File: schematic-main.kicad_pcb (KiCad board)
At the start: 2 copper layers, 97.6 x 72.5 mm, 92 parts, among them IC1 LM76202QPWPRQ1, J1 Conn_01x02, J2 Conn_01x03, J3 Conn_01x03_Pin, J6 Conn_01x04, P1 USB_C_Plug_USB2.0, U2 TPS62933, U3 USBLC6-2P6, U4 ESP32-S3FN8, U5 SN65HVD232, U6 PC817, U7 PC817, Y1 Crystal_GND24

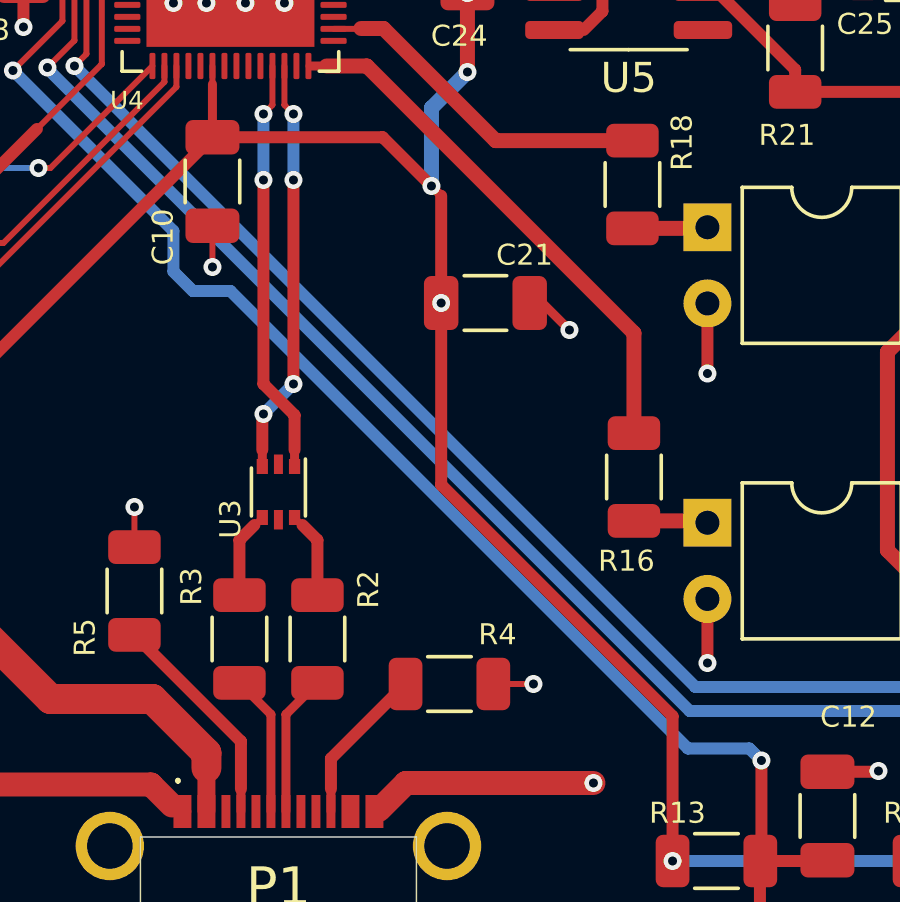
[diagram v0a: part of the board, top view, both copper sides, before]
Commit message: Fixing mistake in control of USB at PCB layout
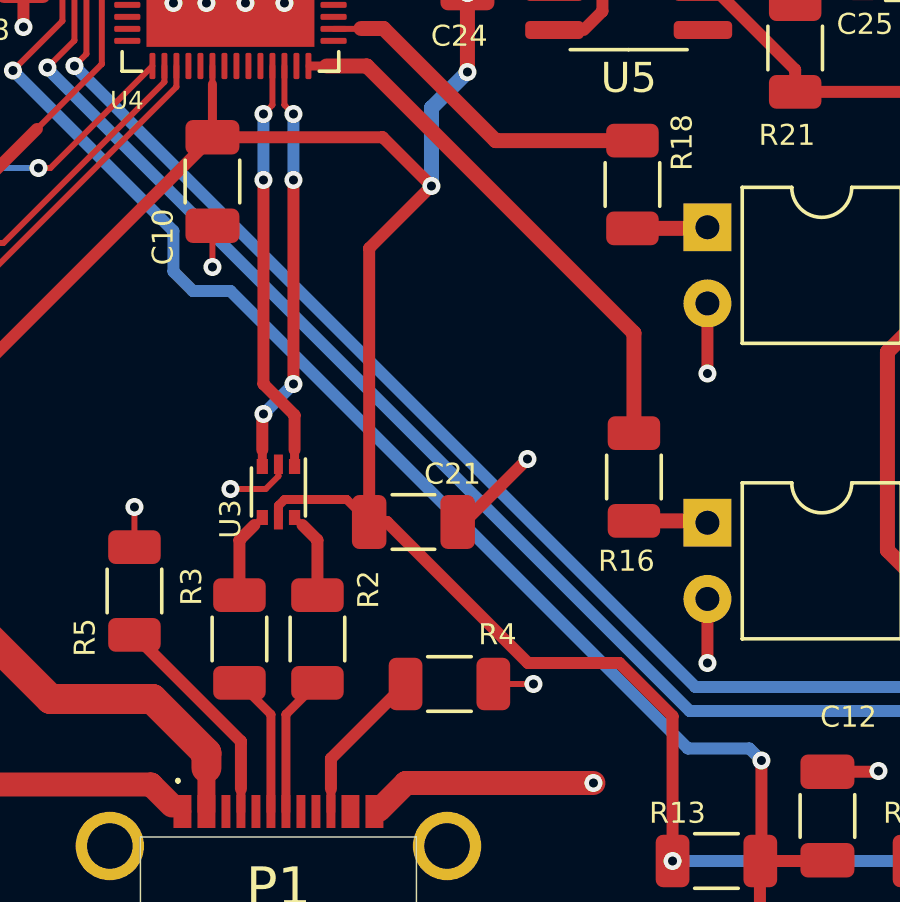
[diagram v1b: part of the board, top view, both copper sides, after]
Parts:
- moved C21 7.68 mm to (107.1, 107.6)
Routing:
- net +3.3V: track 215.0 -> 222.6 mm, vias 11 -> 10
- net GND: track 114.7 -> 118.3 mm, vias 51 -> 52
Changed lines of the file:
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@@
   )
   (footprint "Capacitor_SMD:C_1206_3216Metric" (layer "F.Cu")
-    (at 109.5 100.3)
+    (at 107.1 107.6)
     (descr "Capacitor SMD 1206 (3216 Metric), square (rectangular) end terminal, IPC_7351 nominal, (Body size source: IPC-SM-782 page 76, https://www.pcb-3d.com/wordpress/wp-content/uploads/ipc-sm-782a_amendment_1_and_2.pdf), generated with kicad-footprint-generator")
     (tags "capacitor")
@@
   (segment (start 126.0125 80.4) (end 127.8 80.4) (width 0.4) (layer "F.Cu") (net 2))
   (segment (start 128.8 115.925) (end 130.475 115.925) (width 0.4) (layer "F.Cu") (net 2))
-  (segment (start 110.975 100.3) (end 111.4 100.3) (width 0.3) (layer "F.Cu") (net 2))
   (segment (start 99.25 78.1375) (end 99.25 78.4375) (width 0.2) (layer "F.Cu") (net 2))
   (segment (start 100.4 97.725) (end 100.4 99.1) (width 0.2) (layer "F.Cu") (net 2))
   (segment (start 97.975 82.1375) (end 96.6375 82.1375) (width 0.15) (layer "F.Cu") (net 2))
   (segment (start 101.1625 88.9625) (end 101.2 89) (width 0.15) (layer "F.Cu") (net 2))
+  (segment (start 102.6 105.675) (end 102.6 106.074264) (width 0.2) (layer "F.Cu") (net 2))
   (segment (start 115.737 64.9) (end 114.762 65.875) (width 0.4) (layer "F.Cu") (net 2))
   (segment (start 108.5 58.825) (end 106.825 58.825) (width 0.3) (layer "F.Cu") (net 2))
@@
   (segment (start 108.9 87.02) (end 107.27 87.02) (width 0.4) (layer "F.Cu") (net 2))
   (segment (start 92.125 80.8) (end 92.125 78.925) (width 0.4) (layer "F.Cu") (net 2))
-  (segment (start 111.4 100.3) (end 112.3 101.2) (width 0.3) (layer "F.Cu") (net 2))
   (segment (start 97.975 79.7125) (end 97.975 82.1375) (width 0.3) (layer "F.Cu") (net 2))
   (segment (start 92.125 78.925) (end 92.15 78.9) (width 0.2) (layer "F.Cu") (net 2))
   (segment (start 99.25 117.25) (end 99.05 117.05) (width 0.3) (layer "F.Cu") (net 2))
+  (segment (start 108.8 107.6) (end 110.9 105.5) (width 0.4) (layer "F.Cu") (net 2))
   (segment (start 111.824 66.2) (end 114.437 66.2) (width 0.4) (layer "F.Cu") (net 2))
   (segment (start 106.825 58.825) (end 106.8 58.8) (width 0.3) (layer "F.Cu") (net 2))
@@
   (segment (start 123 64.825) (end 123 63.4) (width 0.3) (layer "F.Cu") (net 2))
   (segment (start 99.25 78.1375) (end 99.25 77.9375) (width 0.2) (layer "F.Cu") (net 2))
+  (segment (start 102.174264 106.5) (end 101 106.5) (width 0.2) (layer "F.Cu") (net 2))
   (segment (start 94.1 89.725) (end 94.1 91.1) (width 0.4) (layer "F.Cu") (net 2))
   (segment (start 81.15 64.7875) (end 81.15 63.4) (width 0.3) (layer "F.Cu") (net 2))
@@
   (segment (start 115.087 66.2) (end 114.762 65.875) (width 0.4) (layer "F.Cu") (net 2))
   (segment (start 92.1 116.35) (end 92.1 116.4) (width 0.8) (layer "F.Cu") (net 2))
+  (segment (start 108.575 107.6) (end 108.8 107.6) (width 0.4) (layer "F.Cu") (net 2))
   (segment (start 117.7 66.2) (end 115.087 66.2) (width 0.4) (layer "F.Cu") (net 2))
   (segment (start 116.821814 63.6) (end 114.762 65.659814) (width 0.4) (layer "F.Cu") (net 2))
@@
   (segment (start 110.54 88.66) (end 111.8 88.66) (width 0.4) (layer "F.Cu") (net 2))
   (segment (start 115 58.8375) (end 116.6625 58.8375) (width 0.3) (layer "F.Cu") (net 2))
+  (segment (start 102.6 106.074264) (end 102.174264 106.5) (width 0.2) (layer "F.Cu") (net 2))
   (segment (start 125.8625 75.8) (end 127.45 75.8) (width 0.4) (layer "F.Cu") (net 2))
   (segment (start 116.9 110.165) (end 116.9 112.3) (width 0.4) (layer "F.Cu") (net 2))
@@
   (via (at 81.15 63.4) (size 0.6) (drill 0.3) (layers "F.Cu" "B.Cu") (net 2))
   (via (at 104.8 73.1) (size 0.6) (drill 0.3) (layers "F.Cu" "B.Cu") (net 2))
-  (via (at 112.3 101.2) (size 0.6) (drill 0.3) (layers "F.Cu" "B.Cu") (net 2))
   (via (at 97.8 107.1) (size 0.6) (drill 0.3) (layers "F.Cu" "B.Cu") (net 2))
   (via (at 100.4 99.1) (size 0.6) (drill 0.3) (layers "F.Cu" "B.Cu") (net 2))
@@
   (via (at 99.1 90.3) (size 0.6) (drill 0.3) (layers "F.Cu" "B.Cu") (net 2))
   (via (at 138.6 115.9) (size 0.6) (drill 0.3) (layers "F.Cu" "B.Cu") (net 2))
+  (via (at 110.9 105.5) (size 0.6) (drill 0.3) (layers "F.Cu" "B.Cu") (net 2))
   (via (at 116.9 102.65) (size 0.6) (drill 0.3) (layers "F.Cu" "B.Cu") (net 2))
   (via (at 101.5 88.7) (size 0.6) (drill 0.3) (layers "F.Cu" "B.Cu") (net 2))
@@
   (via (at 103.3 59.6) (size 0.6) (drill 0.3) (layers "F.Cu" "B.Cu") (net 2))
   (via (at 100.2 90.3) (size 0.6) (drill 0.3) (layers "F.Cu" "B.Cu") (net 2))
+  (via (at 101 106.5) (size 0.6) (drill 0.3) (layers "F.Cu" "B.Cu") (net 2))
   (via (at 125.05 91.005) (size 0.6) (drill 0.3) (layers "F.Cu" "B.Cu") (net 2))
   (via (at 94.5 63.45) (size 0.6) (drill 0.3) (layers "F.Cu" "B.Cu") (net 2))
@@
   (segment (start 73.275 66.865) (end 73.29 66.85) (width 0.5) (layer "F.Cu") (net 5))
   (segment (start 73.29 68.035) (end 73.275 68.05) (width 0.2) (layer "F.Cu") (net 5))
-  (segment (start 108.025 96.725) (end 108.025 100.3) (width 0.4) (layer "F.Cu") (net 6))
-  (segment (start 115.7375 114.07255) (end 108.025 106.36005) (width 0.4) (layer "F.Cu") (net 6))
+  (segment (start 102.6 107.525) (end 102.6 107.055024) (width 0.3) (layer "F.Cu") (net 6))
+  (segment (start 105.625 107.6) (end 106.21924 107.6) (width 0.4) (layer "F.Cu") (net 6))
   (segment (start 94.475 72.575) (end 94.5 72.55) (width 0.2) (layer "F.Cu") (net 6))
+  (segment (start 102.805024 106.85) (end 104.875 106.85) (width 0.3) (layer "F.Cu") (net 6))
+  (segment (start 102.6 107.055024) (end 102.805024 106.85) (width 0.3) (layer "F.Cu") (net 6))
   (segment (start 100.4 94.775) (end 100.4 93) (width 0.3) (layer "F.Cu") (net 6))
   (segment (start 87.8 72.6) (end 87.8 76.4) (width 1) (layer "F.Cu") (net 6))
   (segment (start 97.6 83.7) (end 95.075 83.7) (width 0.4) (layer "F.Cu") (net 6))
+  (segment (start 106.21924 107.6) (end 110.91924 112.3) (width 0.4) (layer "F.Cu") (net 6))
   (segment (start 78.625 72.65) (end 78.65 72.675) (width 0.2) (layer "F.Cu") (net 6))
   (segment (start 107 71.7) (end 98.8 71.7) (width 0.8) (layer "F.Cu") (net 6))
@@
   (segment (start 79.4 86.8) (end 86.075 86.8) (width 0.4) (layer "F.Cu") (net 6))
   (segment (start 98.4 84.5) (end 97.6 83.7) (width 0.4) (layer "F.Cu") (net 6))
+  (segment (start 113.96495 112.3) (end 115.7375 114.07255) (width 0.4) (layer "F.Cu") (net 6))
   (segment (start 98.8 85.45) (end 98.4 85.05) (width 0.2) (layer "F.Cu") (net 6))
   (segment (start 108.9 92.6) (end 108.9 89.97) (width 0.5) (layer "F.Cu") (net 6))
   (segment (start 108.9 89.97) (end 111.76 89.97) (width 0.4) (layer "F.Cu") (net 6))
-  (segment (start 107.7 96.4) (end 108.025 96.725) (width 0.3) (layer "F.Cu") (net 6))
   (segment (start 106.075 94.775) (end 100.4 94.775) (width 0.4) (layer "F.Cu") (net 6))
   (segment (start 131.7375 118.9) (end 131.7 118.9) (width 0.4) (layer "F.Cu") (net 6))
@@
   (segment (start 78.575 72.7) (end 78.65 72.775) (width 0.2) (layer "F.Cu") (net 6))
   (segment (start 81.1875 72.675) (end 81.2 72.6625) (width 0.2) (layer "F.Cu") (net 6))
+  (segment (start 110.91924 112.3) (end 113.96495 112.3) (width 0.4) (layer "F.Cu") (net 6))
   (segment (start 79.125 78.6) (end 81.8 78.6) (width 0.5) (layer "F.Cu") (net 6))
   (segment (start 95.075 80.8) (end 95.075 78.675) (width 0.4) (layer "F.Cu") (net 6))
@@
   (segment (start 75.075 78.6) (end 79.125 78.6) (width 0.4) (layer "F.Cu") (net 6))
   (segment (start 94.5 72.55) (end 87.85 72.55) (width 0.4) (layer "F.Cu") (net 6))
-  (segment (start 108.025 106.36005) (end 108.025 100.3) (width 0.4) (layer "F.Cu") (net 6))
+  (segment (start 105.625 98.475) (end 105.625 107.6) (width 0.4) (layer "F.Cu") (net 6))
   (segment (start 111.76 89.97) (end 111.8 89.93) (width 0.2) (layer "F.Cu") (net 6))
   (segment (start 100.4 92.4) (end 100.4 93) (width 0.2) (layer "F.Cu") (net 6))
+  (segment (start 107.7 96.4) (end 105.625 98.475) (width 0.4) (layer "F.Cu") (net 6))
   (segment (start 87.8 76.4) (end 88.45 77.05) (width 0.8) (layer "F.Cu") (net 6))
   (segment (start 87.85 72.55) (end 87.8 72.6) (width 0.2) (layer "F.Cu") (net 6))
@@
   (segment (start 81.8 78.6) (end 87.8 72.6) (width 0.5) (layer "F.Cu") (net 6))
   (segment (start 105.7 82.725) (end 107.525 80.9) (width 0.5) (layer "F.Cu") (net 6))
+  (segment (start 104.875 106.85) (end 105.625 107.6) (width 0.3) (layer "F.Cu") (net 6))
   (segment (start 88.8 86.825) (end 86.1 86.825) (width 0.4) (layer "F.Cu") (net 6))
   (segment (start 95.075 83.7) (end 95.075 80.8) (width 0.4) (layer "F.Cu") (net 6))
@@
   (via (at 90.5 104.7) (size 0.6) (drill 0.3) (layers "F.Cu" "B.Cu") (net 6))
   (via (at 123.6375 118.9) (size 0.6) (drill 0.3) (layers "F.Cu" "B.Cu") (net 6))
-  (via (at 108.025 100.3) (size 0.6) (drill 0.3) (layers "F.Cu" "B.Cu") (net 6))
   (via (at 87.6 108.2) (size 0.6) (drill 0.3) (layers "F.Cu" "B.Cu") (net 6))
   (via (at 123.6375 118.9) (size 0.6) (drill 0.3) (layers "F.Cu" "B.Cu") (net 6))
@@
   (segment (start 107.7 93.8) (end 107.7 96.4) (width 0.5) (layer "B.Cu") (net 6))
   (segment (start 105.7 86.77) (end 108.9 89.97) (width 0.5) (layer "B.Cu") (net 6))
-  (segment (start 107.963 100.362) (end 108.025 100.3) (width 0.3) (layer "B.Cu") (net 6))
   (segment (start 105.7 82.75) (end 105.7 86.77) (width 0.5) (layer "B.Cu") (net 6))
   (segment (start 123.6375 118.9) (end 115.7375 118.9) (width 0.4) (layer "B.Cu") (net 6))
